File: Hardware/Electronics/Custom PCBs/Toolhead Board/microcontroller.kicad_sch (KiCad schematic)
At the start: 27 parts, among them U3 W25Q128JVS, U5 RP2040, Y1 12MHz/12pF/50Ω/20ppm

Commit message: Work on Toolhead Board
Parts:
- removed R4, R5: 27.4, Resistor_SMD:R_0402_1005Metric, symbol Device:R
- added J2: USB C Receptacle, Connector_USB:USB_C_Receptacle_G-Switch_GT-USB-7010ASV, symbol Connector:USB_C_Receptacle_USB2.0
- added R10, R11: 5.1k, Resistor_SMD:R_0402_1005Metric, symbol Device:R
- added R2, R3: 27.4, Resistor_SMD:R_0402_1005Metric, symbol Device:R
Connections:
- net GND: now also J2.A1 (GND), J2.A12 (GND), J2.B1 (GND), J2.B12 (GND), J2.S1 (SHIELD), R10.2, R11.2
- net USB-: now reaches U5.46 (USB_DM)
- net USB-: now also R3.1
- net USB+: now reaches U5.47 (USB_DP)
- net USB+: now also R2.2
- net ADC3 renamed MOT_DIAG
- net D13 renamed LED
- net D17 renamed MOT_EN
- net D18 renamed MOT_STP
- net D19 renamed MOT_DIR
- net D20 renamed MOT_UART
- net D4 renamed CAN_TX
- net D5 renamed CAN_RX
- net D6 renamed CAN_S
- new net: J2.A6 (D+), J2.B6 (D+), R3.2
- new net: J2.A7 (D-), J2.B7 (D-), R2.1
- new net: J2.B5 (CC2), R10.1
- new net: J2.A5 (CC1), R11.1
- new net VBUS: J2.A4 (VBUS), J2.A9 (VBUS), J2.B4 (VBUS), J2.B9 (VBUS)
- no-connect marks 2 -> 4
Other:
- note added: "USB Connector"
- moved on the sheet: C14, R1, R2, U3

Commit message: some updates
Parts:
- BOOT1, RESET1: footprint Button_Switch_SMD:SW_SPST_B3U-1000P -> (none); LCSC C231329 -> (none)
- C1, C15, C16, C2, C3, C4, C5, C6, C7, C8, C9: footprint Capacitor_SMD:C_0402_1005Metric -> (none)
- C14: footprint Capacitor_SMD:C_0402_1005Metric -> (none); LCSC C915972 -> (none)
- C20, C21: footprint Capacitor_SMD:C_0402_1005Metric -> (none); LCSC C2185179 -> (none)
- D1: footprint LED_SMD:LED_0402_1005Metric -> (none); LCSC C401113 -> (none)
- J2: footprint Connector_USB:USB_C_Receptacle_G-Switch_GT-USB-7010ASV -> (none); Digikey (none) -> 664-12402012E212ACT-ND; LCSC C2988369 -> (none)
- R1, R3, R6: footprint Resistor_SMD:R_0402_1005Metric -> (none); LCSC C153109 -> (none)
- R10, R11: footprint Resistor_SMD:R_0402_1005Metric -> (none); LCSC C2906948 -> (none)
- R2, R7: footprint Resistor_SMD:R_0402_1005Metric -> (none); LCSC C98841 -> (none)
- R2, R3: footprint Resistor_SMD:R_0402_1005Metric -> (none)
- U3: footprint Package_SO:SOIC-8_5.23x5.23mm_P1.27mm -> (none); Digikey (none) -> W25Q128JVSIQ-ND; LCSC C97521 -> (none)
- U5: footprint Package_DFN_QFN:QFN-56-1EP_7x7mm_P0.4mm_EP3.2x3.2mm -> (none); Digikey (none) -> 2648-SC0914(13)CT-ND
- Y1: footprint Crystal:Crystal_SMD_3225-4Pin_3.2x2.5mm -> (none); LCSC C2450215 -> (none)
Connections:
- net ADC0 renamed STRAIN1_DO
- net ADC1 renamed STRAIN2_DO
- net ADC2 renamed STRAIN3_DO

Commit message: Work on toolhead board more
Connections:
- net D21 is gone; now on net MOT_DIAG: U5.32 (GPIO21)
- net MOT_DIAG: no longer U5.41 (GPIO29_ADC3)
- net D2 renamed SDA
- net D3 renamed SCL
- new net STRAIN_SCK: U5.41 (GPIO29_ADC3)
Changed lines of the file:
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@@
+    (stroke (width 0) (type default))
+  )
+  (wire (pts (xy 125.73 91.44) (xy 111.76 91.44))
     (stroke (width 0) (type default))
   )
@@
     (effects (font (size 1.27 1.27)) (justify left bottom))
   )
+  (label "LED" (at 125.73 91.44 180) (fields_autoplaced)
+    (effects (font (size 1.27 1.27)) (justify right bottom))
+  )
   (label "QSPI_SD3" (at 60.96 88.9 180) (fields_autoplaced)
     (effects (font (size 1.27 1.27)) (justify right bottom))
@@
     (effects (font (size 1.27 1.27)) (justify right bottom))
   )
-  (global_label "D21" (shape input) (at 111.76 111.76 0) (fields_autoplaced)
-    (effects (font (size 1.27 1.27)) (justify left))
-    (property "Intersheetrefs" "${INTERSHEET_REFS}" (at 118.4342 111.76 0)
+  (global_label "MOT_DIAG" (shape input) (at 111.76 111.76 0) (fields_autoplaced)
+    (effects (font (size 1.27 1.27)) (justify left))
+    (property "Intersheetrefs" "${INTERSHEET_REFS}" (at 123.6957 111.76 0)
       (effects (font (size 1.27 1.27)) (justify left) hide)
     )
@@
     )
   )
-  (global_label "D3" (shape input) (at 111.76 66.04 0) (fields_autoplaced)
-    (effects (font (size 1.27 1.27)) (justify left))
-    (property "Intersheetrefs" "${INTERSHEET_REFS}" (at 117.2247 66.04 0)
+  (global_label "SCL" (shape input) (at 111.76 66.04 0) (fields_autoplaced)
+    (effects (font (size 1.27 1.27)) (justify left))
+    (property "Intersheetrefs" "${INTERSHEET_REFS}" (at 118.2528 66.04 0)
       (effects (font (size 1.27 1.27)) (justify left) hide)
     )
@@
     )
   )
-  (global_label "LED" (shape input) (at 111.76 91.44 0) (fields_autoplaced)
-    (effects (font (size 1.27 1.27)) (justify left))
-    (property "Intersheetrefs" "${INTERSHEET_REFS}" (at 118.1923 91.44 0)
-      (effects (font (size 1.27 1.27)) (justify left) hide)
-    )
-  )
-  (global_label "D2" (shape input) (at 111.76 63.5 0) (fields_autoplaced)
-    (effects (font (size 1.27 1.27)) (justify left))
-    (property "Intersheetrefs" "${INTERSHEET_REFS}" (at 117.2247 63.5 0)
+  (global_label "SDA" (shape input) (at 111.76 63.5 0) (fields_autoplaced)
+    (effects (font (size 1.27 1.27)) (justify left))
+    (property "Intersheetrefs" "${INTERSHEET_REFS}" (at 118.3133 63.5 0)
       (effects (font (size 1.27 1.27)) (justify left) hide)
     )
@@
     )
   )
-  (global_label "MOT_DIAG" (shape input) (at 111.76 134.62 0) (fields_autoplaced)
-    (effects (font (size 1.27 1.27)) (justify left))
-    (property "Intersheetrefs" "${INTERSHEET_REFS}" (at 123.6957 134.62 0)
-      (effects (font (size 1.27 1.27)) (justify left) hide)
-    )
+  (global_label "STRAIN_SCK" (shape input) (at 111.76 134.62 0) (fields_autoplaced)
+    (effects (font (size 1.27 1.27)) (justify left))
+    (property "Intersheetrefs" "${INTERSHEET_REFS}" (at 125.9333 134.62 0)
+      (effects (font (size 1.27 1.27)) (justify left) hide)
+    )

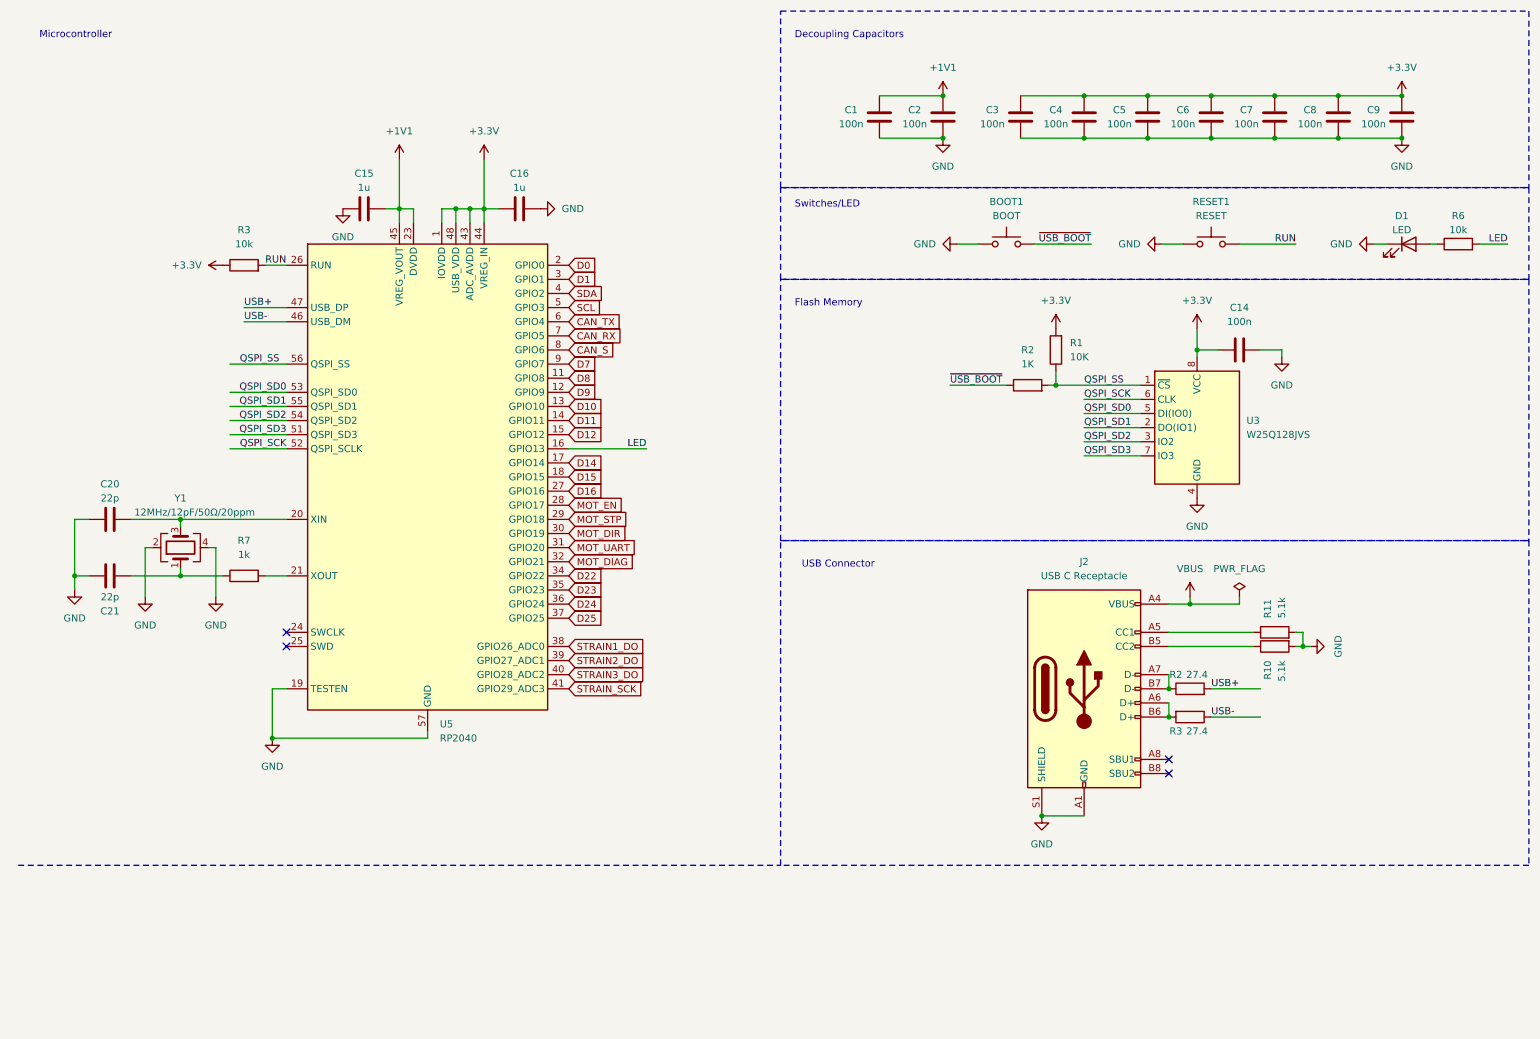
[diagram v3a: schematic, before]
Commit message: Finish Toolhead Schematic
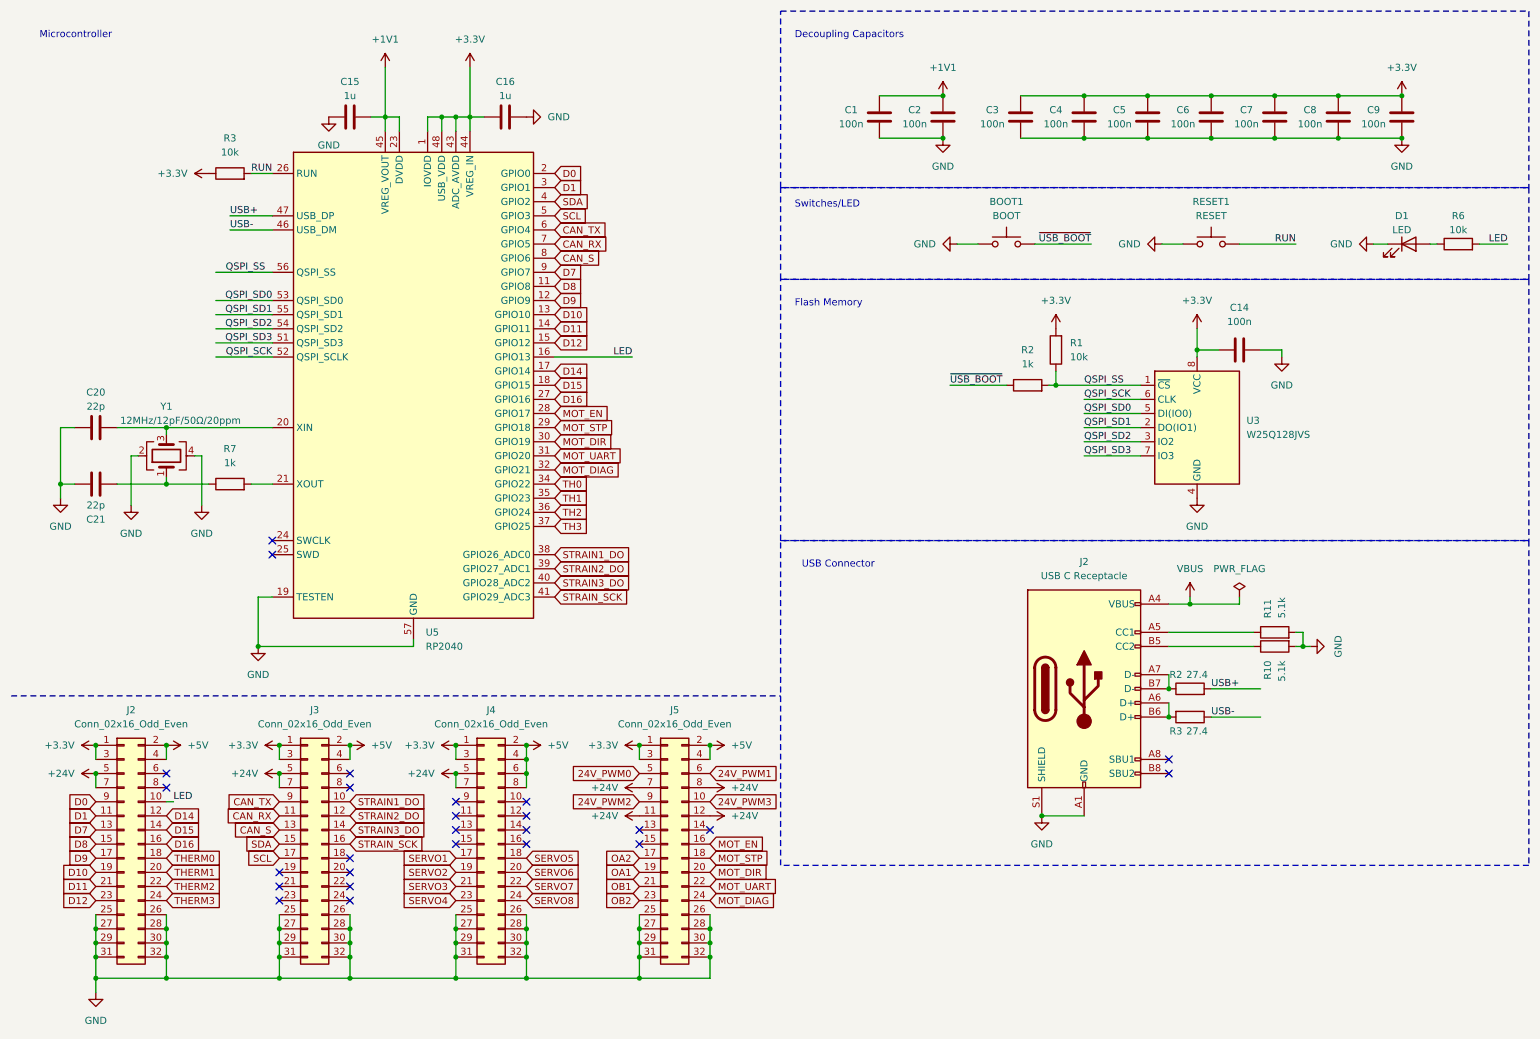
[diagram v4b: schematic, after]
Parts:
- added J2, J3, J4, J5: Conn_02x16_Odd_Even, symbol Connector_Generic:Conn_02x16_Odd_Even
- BOOT1, RESET1: footprint (none) -> Button_Switch_SMD:SW_SPST_B3U-1000P; Digikey (none) -> SW1020CT-ND
- C1, C14, C2, C3, C4, C5, C6, C7, C8, C9: Digikey (none) -> 1276-1935-1-ND
- C15, C16: Digikey (none) -> 1276-1102-1-ND
- C20, C21: Digikey (none) -> 478-KGM15ACG1C220KTCT-ND
- R1: value 10K -> 10k; footprint (none) -> Resistor_SMD:R_0603_1608Metric_Pad0.98x0.95mm_HandSolder; Digikey (none) -> 1292-WR06X103JTLCT-ND
- R10, R11: footprint (none) -> Resistor_SMD:R_0603_1608Metric_Pad0.98x0.95mm_HandSolder; Digikey (none) -> 311-5.10KHRCT-ND
- R2: value 1K -> 1k; footprint (none) -> Resistor_SMD:R_0603_1608Metric_Pad0.98x0.95mm_HandSolder; Digikey (none) -> 311-1.00KHRCT-ND
- R2, R3: footprint (none) -> Resistor_SMD:R_0603_1608Metric_Pad0.98x0.95mm_HandSolder; Digikey (none) -> RMCF0603FT27R4CT-ND
- R3, R6: footprint (none) -> Resistor_SMD:R_0603_1608Metric_Pad0.98x0.95mm_HandSolder; Digikey (none) -> 1292-WR06X103JTLCT-ND
- R7: footprint (none) -> Resistor_SMD:R_0603_1608Metric_Pad0.98x0.95mm_HandSolder; Digikey (none) -> 311-1.00KHRCT-ND
- Y1: Digikey (none) -> XC1426CT-ND
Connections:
- net +3.3V: now also J2.1 (Pin_1), J2.3 (Pin_3), J3.1 (Pin_1), J3.3 (Pin_3), J4.1 (Pin_1), J4.3 (Pin_3), J5.1 (Pin_1), J5.3 (Pin_3)
- net CAN_RX: now also J3.11 (Pin_11)
- net CAN_S: now also J3.13 (Pin_13)
- net CAN_TX: now also J3.9 (Pin_9)
- net D0: now also J2.9 (Pin_9)
- net D1: now also J2.11 (Pin_11)
- net D10: now also J2.19 (Pin_19)
- net D11: now also J2.21 (Pin_21)
- net D12: now also J2.23 (Pin_23)
- net D14: now also J2.12 (Pin_12)
- net D15: now also J2.14 (Pin_14)
- net D16: now also J2.16 (Pin_16)
- net D7: now also J2.13 (Pin_13)
- net D8: now also J2.15 (Pin_15)
- net D9: now also J2.17 (Pin_17)
- net GND: now also J2.25 (Pin_25), J2.26 (Pin_26), J2.27 (Pin_27), J2.28 (Pin_28), J2.29 (Pin_29), J2.30 (Pin_30), J2.31 (Pin_31), J2.32 (Pin_32), J3.25 (Pin_25), J3.26 (Pin_26), J3.27 (Pin_27), J3.28 (Pin_28), J3.29 (Pin_29), J3.30 (Pin_30), J3.31 (Pin_31), J3.32 (Pin_32), J4.25 (Pin_25), J4.26 (Pin_26), J4.27 (Pin_27), J4.28 (Pin_28), J4.29 (Pin_29), J4.30 (Pin_30), J4.31 (Pin_31), J4.32 (Pin_32), J5.25 (Pin_25), J5.26 (Pin_26), J5.27 (Pin_27), J5.28 (Pin_28), J5.29 (Pin_29), J5.30 (Pin_30), J5.31 (Pin_31), J5.32 (Pin_32)
- net LED: now also J2.10 (Pin_10)
- net MOT_DIAG: now also J5.24 (Pin_24)
- net MOT_DIR: now also J5.20 (Pin_20)
- net MOT_EN: now also J5.16 (Pin_16)
- net MOT_STP: now also J5.18 (Pin_18)
- net MOT_UART: now also J5.22 (Pin_22)
- net SCL: now also J3.17 (Pin_17)
- net SDA: now also J3.15 (Pin_15)
- net STRAIN1_DO: now also J3.10 (Pin_10)
- net STRAIN2_DO: now also J3.12 (Pin_12)
- net STRAIN3_DO: now also J3.14 (Pin_14)
- net STRAIN_SCK: now also J3.16 (Pin_16)
- net D22 renamed TH0
- net D23 renamed TH1
- net D24 renamed TH2
- net D25 renamed TH3
- new net +24V: J2.5 (Pin_5), J2.7 (Pin_7), J3.5 (Pin_5), J3.7 (Pin_7), J4.5 (Pin_5), J4.7 (Pin_7), J5.11 (Pin_11), J5.12 (Pin_12), J5.7 (Pin_7), J5.8 (Pin_8)
- new net +5V: J2.2 (Pin_2), J2.4 (Pin_4), J3.2 (Pin_2), J3.4 (Pin_4), J4.2 (Pin_2), J4.4 (Pin_4), J4.6 (Pin_6), J4.8 (Pin_8), J5.2 (Pin_2), J5.4 (Pin_4)
- new net 24V_PWM0: J5.5 (Pin_5)
- new net 24V_PWM1: J5.6 (Pin_6)
- new net 24V_PWM2: J5.9 (Pin_9)
- new net 24V_PWM3: J5.10 (Pin_10)
- new net OA1: J5.19 (Pin_19)
- new net OA2: J5.17 (Pin_17)
- new net OB1: J5.21 (Pin_21)
- new net OB2: J5.23 (Pin_23)
- new net SERVO1: J4.17 (Pin_17)
- new net SERVO2: J4.19 (Pin_19)
- new net SERVO3: J4.21 (Pin_21)
- new net SERVO4: J4.23 (Pin_23)
- new net SERVO5: J4.18 (Pin_18)
- new net SERVO6: J4.20 (Pin_20)
- new net SERVO7: J4.22 (Pin_22)
- new net SERVO8: J4.24 (Pin_24)
- new net THERM0: J2.18 (Pin_18)
- new net THERM1: J2.20 (Pin_20)
- new net THERM2: J2.22 (Pin_22)
- new net THERM3: J2.24 (Pin_24)
- no-connect marks 4 -> 26
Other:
- moved on the sheet: C15, C16, C20, C21, R3, R7, U5, Y1

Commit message: Updated Footprints
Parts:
- C10: renamed from C4; footprint (none) -> Capacitor_SMD:C_0603_1608Metric_Pad1.08x0.95mm_HandSolder
- C11: renamed from C5; footprint (none) -> Capacitor_SMD:C_0603_1608Metric_Pad1.08x0.95mm_HandSolder
- C12: renamed from C6; footprint (none) -> Capacitor_SMD:C_0603_1608Metric_Pad1.08x0.95mm_HandSolder
- C13: renamed from C7; footprint (none) -> Capacitor_SMD:C_0603_1608Metric_Pad1.08x0.95mm_HandSolder
- C14: renamed from C8; footprint (none) -> Capacitor_SMD:C_0603_1608Metric_Pad1.08x0.95mm_HandSolder
- C15: renamed from C9; footprint (none) -> Capacitor_SMD:C_0603_1608Metric_Pad1.08x0.95mm_HandSolder
- C16: renamed from C14; footprint (none) -> Capacitor_SMD:C_0603_1608Metric_Pad1.08x0.95mm_HandSolder
- C5: renamed from C15; footprint (none) -> Capacitor_SMD:C_0603_1608Metric_Pad1.08x0.95mm_HandSolder
- C6: renamed from C16; footprint (none) -> Capacitor_SMD:C_0603_1608Metric_Pad1.08x0.95mm_HandSolder
- C7: renamed from C1; footprint (none) -> Capacitor_SMD:C_0603_1608Metric_Pad1.08x0.95mm_HandSolder
- C8: renamed from C2; footprint (none) -> Capacitor_SMD:C_0603_1608Metric_Pad1.08x0.95mm_HandSolder
- C9: renamed from C3; footprint (none) -> Capacitor_SMD:C_0603_1608Metric_Pad1.08x0.95mm_HandSolder
- U3: renamed from U5; footprint (none) -> Package_DFN_QFN:QFN-56-1EP_7x7mm_P0.4mm_EP3.2x3.2mm
- renumbered C20 to C17, C21 to C18, J2 to J1, R3 to R1, R6 to R2, R1 to R3, R2 to R4, R7 to R5, R11 to R6, R10 to R7, R2 to R8, R3 to R9, BOOT1 to SW1, RESET1 to SW2, U3 to U4

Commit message: Continue adding footprints
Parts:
- C17, C18: footprint (none) -> Capacitor_SMD:C_0603_1608Metric_Pad1.08x0.95mm_HandSolder
- D1: footprint (none) -> LED_SMD:LED_1206_3216Metric_Pad1.42x1.75mm_HandSolder
- J1: footprint (none) -> usb_port:12402012E212A_AMP
- J2, J3, J4, J5: footprint (none) -> Connector_PinHeader_2.54mm:PinHeader_2x16_P2.54mm_Vertical
- U4: footprint (none) -> Package_SO:SOIC-8_5.23x5.23mm_P1.27mm
- Y1: footprint (none) -> Oscillator:Oscillator_SMD_SeikoEpson_SG210-4Pin_2.5x2.0mm_HandSoldering
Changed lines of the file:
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@@
 			)
 		)
-		(property "Footprint" ""
+		(property "Footprint" "Connector_PinHeader_2.54mm:PinHeader_2x16_P2.54mm_Vertical"
 			(at 64.77 162.56 0)
 			(effects
@@
 			)
 		)
-		(property "Footprint" ""
+		(property "Footprint" "Oscillator:Oscillator_SMD_SeikoEpson_SG210-4Pin_2.5x2.0mm_HandSoldering"
 			(at 39.37 92.71 0)
 			(effects
@@
 			)
 		)
-		(property "Footprint" ""
+		(property "Footprint" "Connector_PinHeader_2.54mm:PinHeader_2x16_P2.54mm_Vertical"
 			(at 129.54 162.56 0)
 			(effects
@@
 			)
 		)
-		(property "Footprint" ""
+		(property "Footprint" "Capacitor_SMD:C_0603_1608Metric_Pad1.08x0.95mm_HandSolder"
 			(at 30.48 98.7552 0)
 			(effects
@@
 			)
 		)
-		(property "Footprint" ""
+		(property "Footprint" "Capacitor_SMD:C_0603_1608Metric_Pad1.08x0.95mm_HandSolder"
 			(at 30.48 86.6648 0)
 			(effects
@@
 			)
 		)
-		(property "Footprint" ""
+		(property "Footprint" "Connector_PinHeader_2.54mm:PinHeader_2x16_P2.54mm_Vertical"
 			(at 31.75 162.56 0)
 			(effects
@@
 			)
 		)
-		(property "Footprint" ""
+		(property "Footprint" "Package_SO:SOIC-8_5.23x5.23mm_P1.27mm"
 			(at 224.79 87.63 0)
 			(effects
@@
 			)
 		)
-		(property "Footprint" ""
+		(property "Footprint" "Connector_PinHeader_2.54mm:PinHeader_2x16_P2.54mm_Vertical"
 			(at 96.52 162.56 0)
 			(effects
@@
 			)
 		)
-		(property "Footprint" ""
+		(property "Footprint" "usb_port:12402012E212A_AMP"
 			(at 208.28 134.62 0)
 			(effects
@@
 			)
 		)
-		(property "Footprint" ""
+		(property "Footprint" "LED_SMD:LED_1206_3216Metric_Pad1.42x1.75mm_HandSolder"
 			(at 262.89 54.61 0)
 			(effects

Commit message: Get basic Toolhead Board outline
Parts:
- removed J2, J3, J4, J5: Conn_02x16_Odd_Even, Connector_PinHeader_2.54mm:PinHeader_2x16_P2.54mm_Vertical, symbol Connector_Generic:Conn_02x16_Odd_Even
- added J2, J3, J4: Conn_02x08_Odd_Even, Connector_PinSocket_2.54mm:PinSocket_2x08_P2.54mm_Vertical, symbol Connector_Generic:Conn_02x08_Odd_Even
- added J5, J6: Conn_02x04_Odd_Even, Connector_PinSocket_2.54mm:PinSocket_2x04_P2.54mm_Vertical, symbol Connector_Generic:Conn_02x04_Odd_Even
- J1: footprint usb_port:12402012E212A_AMP -> Connector_USB:USB_C_Receptacle_GCT_USB4105-xx-A_16P_TopMnt_Horizontal
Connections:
- net +24V: now also J3.3 (Pin_3), J4.3 (Pin_3), J5.3 (Pin_3), J5.4 (Pin_4)
- net +3.3V: now also J2.1 (Pin_1), J3.1 (Pin_1), J4.1 (Pin_1), J5.1 (Pin_1)
- net +5V: now also J2.2 (Pin_2), J3.2 (Pin_2), J4.2 (Pin_2), J4.4 (Pin_4), J5.2 (Pin_2)
- net 24V_PWM0: now also J5.5 (Pin_5)
- net 24V_PWM1: now also J5.6 (Pin_6)
- net 24V_PWM2: now also J5.7 (Pin_7)
- net 24V_PWM3: now also J5.8 (Pin_8)
- net CAN_RX: now also J3.7 (Pin_7)
- net CAN_S: now also J3.9 (Pin_9)
- net CAN_TX: now also J3.5 (Pin_5)
- net D0: now also J2.3 (Pin_3)
- net D1: now also J2.5 (Pin_5)
- net D10: now also J2.13 (Pin_13)
- net D11: now also J2.14 (Pin_14)
- net D12: now also J2.6 (Pin_6)
- net D14: now also J2.8 (Pin_8)
- net D15: now also J2.10 (Pin_10)
- net D16: now also J2.12 (Pin_12)
- net D7: now also J2.7 (Pin_7)
- net D8: now also J2.9 (Pin_9)
- net D9: now also J2.11 (Pin_11)
- net GND: now also J2.15 (Pin_15), J2.16 (Pin_16), J3.13 (Pin_13), J3.14 (Pin_14), J3.15 (Pin_15), J3.16 (Pin_16), J4.13 (Pin_13), J4.14 (Pin_14), J4.15 (Pin_15), J4.16 (Pin_16), J6.7 (Pin_7), J6.8 (Pin_8)
- net LED: now also J2.4 (Pin_4)
- net OA1: now also J6.3 (Pin_3)
- net OA2: now also J6.1 (Pin_1)
- net OB1: now also J6.2 (Pin_2)
- net OB2: now also J6.4 (Pin_4)
- net SCL: now also J3.12 (Pin_12)
- net SDA: now also J3.11 (Pin_11)
- net SERVO1: now also J4.5 (Pin_5)
- net SERVO2: now also J4.7 (Pin_7)
- net SERVO3: now also J4.9 (Pin_9)
- net SERVO4: now also J4.11 (Pin_11)
- net SERVO5: now also J4.6 (Pin_6)
- net SERVO6: now also J4.8 (Pin_8)
- net SERVO7: now also J4.10 (Pin_10)
- net SERVO8: now also J4.12 (Pin_12)
- net THERM0: now also J3.4 (Pin_4)
- net THERM1: now also J3.6 (Pin_6)
- net THERM2: now also J3.8 (Pin_8)
- net THERM3: now also J3.10 (Pin_10)
- no-connect marks 26 -> 4
